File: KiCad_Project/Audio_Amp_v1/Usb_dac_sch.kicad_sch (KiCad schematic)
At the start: 40 parts, among them J1 Screw_Terminal_01x02, J2 Screw_Terminal_01x02, J3 Barrel_Jack_Switch, J6 USB_C_Receptacle_USB2.0_16P, Q1 NMOS, U1 PCM2704CDB, U2 USBLC6-2SC6, U4 L78L12_SOT89, Y1 12Mhz

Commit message: Started routing
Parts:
- removed C34: 10u, EEE-FK1H221GV:EEHZT1E561UV, symbol Device:C_Polarized_US
- removed Q1: NMOS, symbol Simulation_SPICE:NMOS
- added C34: 10u, Capacitor_SMD:C_0603_1608Metric, symbol Device:C
- added Q2: BSS138, Package_TO_SOT_SMD:SOT-23, symbol Transistor_FET:BSS138
- C30, C46: footprint Capacitor_SMD:C_0603_1608Metric -> Capacitor_SMD:C_0805_2012Metric
- C38, C40: footprint EEE-FK1H221GV:EEHZT1E561UV -> Capacitor_SMD:CP_Elec_4x5.8
- C43: footprint (none) -> PCM_JLCPCB:C_0805
- C44: footprint (none) -> Capacitor_SMD:C_0603_1608Metric
- C45: footprint (none) -> Capacitor_SMD:C_0805_2012Metric
- H1, H2, H3, H4: footprint (none) -> MountingHole:MountingHole_3.2mm_M3_Pad_Via
- J1, J2: footprint (none) -> TerminalBlock_Phoenix:TerminalBlock_Phoenix_MKDS-1,5-2-5.08_1x02_P5.08mm_Horizontal
- J3: footprint (none) -> Connector_BarrelJack:BarrelJack_CUI_PJ-102AH_Horizontal
- J6: footprint (none) -> Connector_USB:USB_C_Receptacle_GCT_USB4105-xx-A_16P_TopMnt_Horizontal
- XC1: renamed from Y1; footprint (none) -> Crystal:Crystal_SMD_HC49-SD; PARTNO (none) -> ECS-120-20-5PX-TR
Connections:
- net DAC_ACTIVE: now also Q2.1 (G)
- net GNDA: now also C34.1, Q2.2 (S)
- net OUT_N_LEFT: now also J2.1 (Pin_1); no longer J2.2 (Pin_2)
- net OUT_N_RIGHT: now also J1.1 (Pin_1); no longer J1.2 (Pin_2)
- net OUT_P_LEFT: now also J2.2 (Pin_2); no longer J2.1 (Pin_1)
- net OUT_P_RIGHT: now also J1.2 (Pin_2); no longer J1.1 (Pin_1)
- net at R17.1, R30.2: now also Q2.3 (D)
- net DAC_D+: now reaches R11.2, U1.9 (D+)
- net DAC_D-: now reaches R10.2, U1.8 (D-)
- net at U1.18 (VCOM): now also C34.2
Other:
- moved on the sheet: R21, TP4

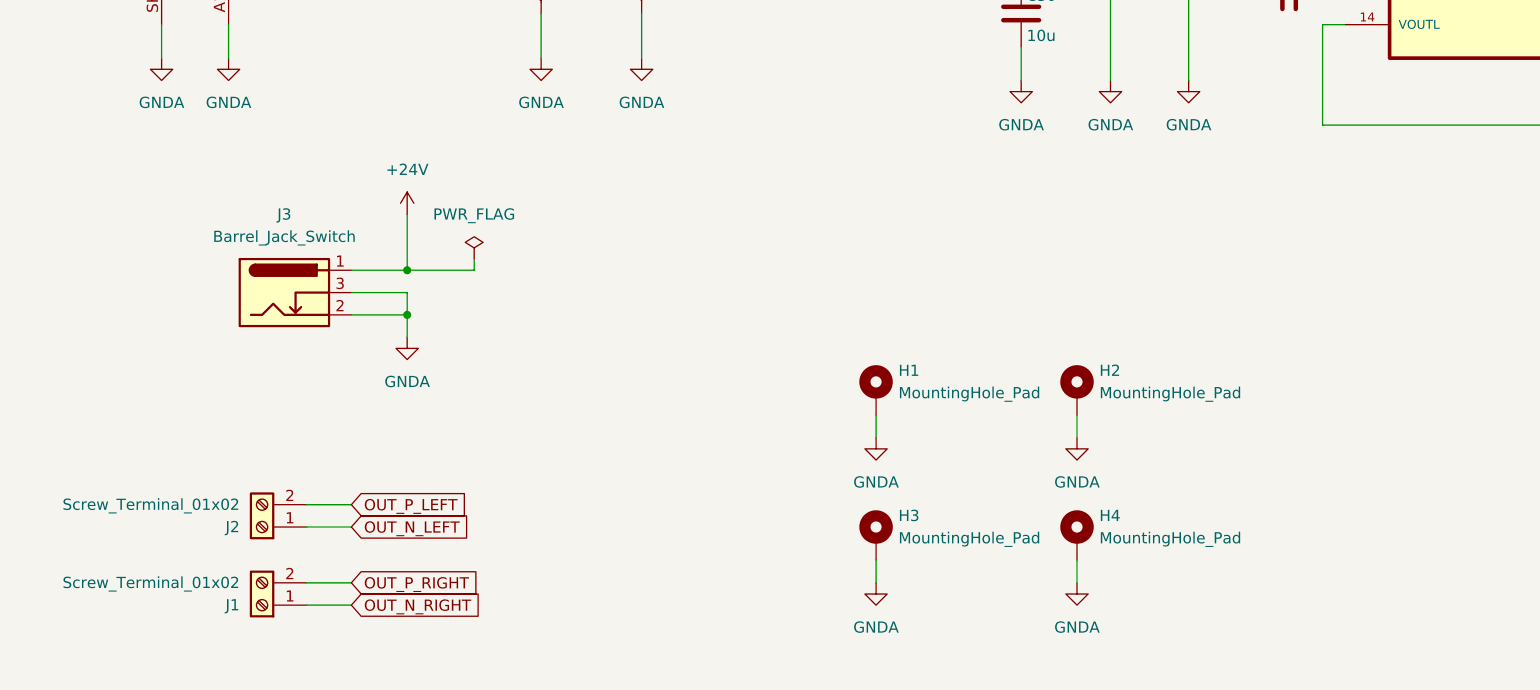
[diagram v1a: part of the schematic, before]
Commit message: added reverse polarity protection
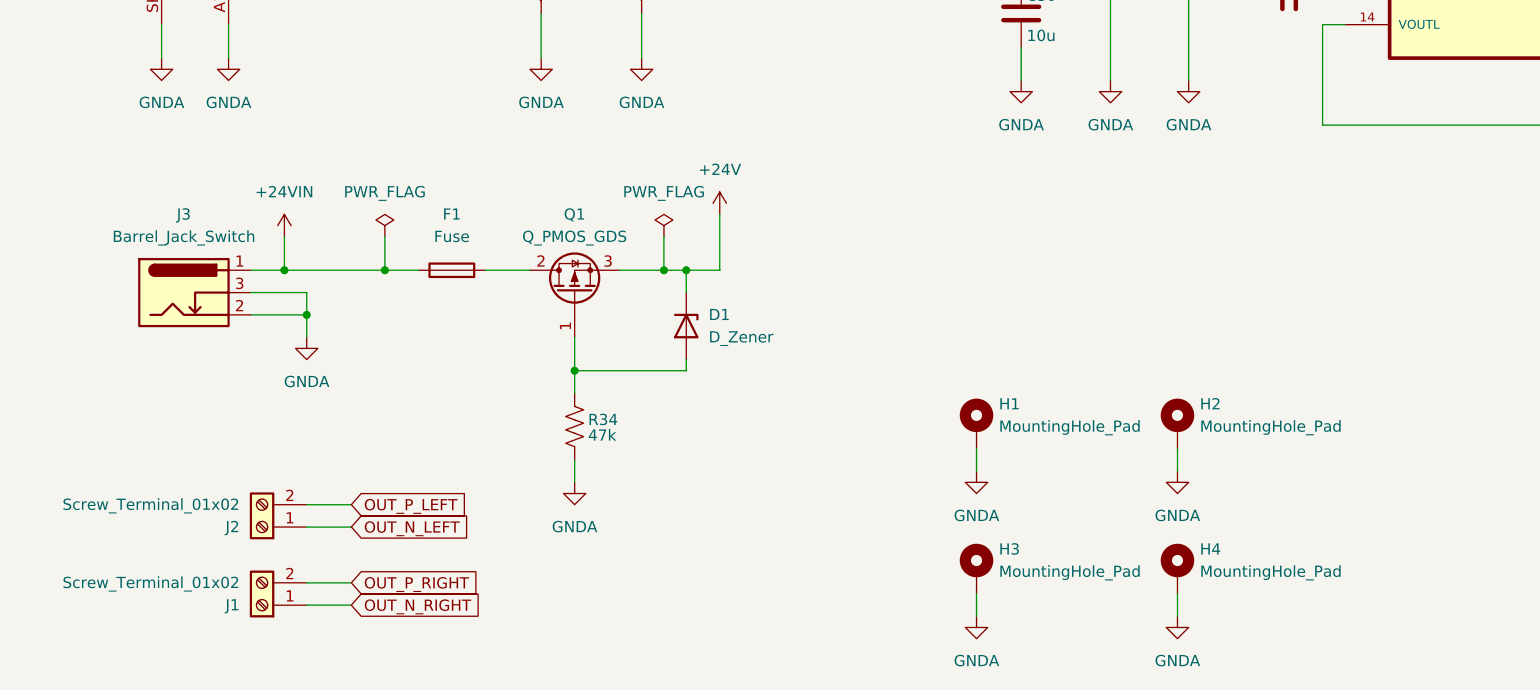
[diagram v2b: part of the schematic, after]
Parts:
- added D1: D_Zener, Diode_SMD:D_SOD-123, symbol Device:D_Zener
- added F1: Fuse, Fuse:Fuse_2920_7451Metric_Pad2.10x5.45mm_HandSolder, symbol Device:Fuse
- added Q1: Q_PMOS_GDS, Package_TO_SOT_SMD:TO-252-2, symbol Transistor_FET:Q_PMOS_GDS
- added R34: 47k, Resistor_SMD:R_0603_1608Metric, symbol Device:R_US
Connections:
- net +24V: now also D1.1 (K), Q1.3 (S); no longer J3.1
- net GNDA: now also R34.2
- new net: F1.2, Q1.2 (D)
- new net: D1.2 (A), Q1.1 (G), R34.1
- new net +24VIN: F1.1, J3.1
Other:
- moved on the sheet: H1, H2, H3, H4, J3

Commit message: Added led into pcb and lyout completed
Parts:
- added D2, D3, D4: LED, LED_SMD:LED_0805_2012Metric, symbol Device:LED
- added R15: 3k3, Resistor_SMD:R_0603_1608Metric, symbol Device:R_US
- added R18: 1k, Resistor_SMD:R_0603_1608Metric, symbol Device:R_US
- C30, C45: LCSC (none) -> C84416
- C32, C33, C37: LCSC (none) -> C5199872
- C34: LCSC (none) -> C962136
- C35, C36: LCSC (none) -> C5137624
- C38, C40: LCSC C116211 -> C445472
- C43: LCSC (none) -> C309049
- C44: LCSC (none) -> C5137636
- C46: LCSC (none) -> C2885646
- D1: LCSC (none) -> C2104
- F1: LCSC (none) -> C22870534
- J1, J2: LCSC (none) -> C480516
- J3: LCSC (none) -> C3096093
- J6: LCSC (none) -> C3020560
- Q1: LCSC (none) -> C513222
- Q2: LCSC (none) -> C52895
- R10, R11: LCSC C25586 -> C23345
- R14: LCSC C25586 -> C2930050
- R16: LCSC (none) -> C2907003
- R17, R19, R21, R34: LCSC C25586 -> C2907042
- R20: LCSC C25586 -> C98220
- R30: LCSC C25586 -> C14675
- R31, R32: LCSC C25586 -> C2907044
- U1: LCSC (none) -> C2859784
- U2: LCSC (none) -> C7519
- U4: LCSC (none) -> C915681
- XC1: LCSC (none) -> C5383154
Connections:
- net +12V: now also D2.2 (A)
- net GNDA: now also R15.2, R18.2
- net VBUS: now also D3.2 (A)
- net at Q2.3 (D), R30.2: now also D4.1 (K); no longer R17.1
- new net: D4.2 (A), R17.1
- new net: D3.1 (K), R18.1
- new net: D2.1 (K), R15.1
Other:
- moved on the sheet: R17

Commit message: added Images folder and changed some relative paths in the Kicad preferences
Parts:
- D3: LCSC C2293 -> C84256
- D4: LCSC C2297 -> C84256
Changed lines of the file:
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@@
 			)
 		)
-		(property "LCSC" "C2297"
+		(property "LCSC" "C84256"
 			(at 247.65 55.88 90)
 			(hide yes)
@@
 			)
 		)
-		(property "LCSC" "C2293"
+		(property "LCSC" "C84256"
 			(at 99.06 66.04 90)
 			(hide yes)

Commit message: Use shared Kicad_Libs instead of project-specific libraries
- Project parts moved to Kicad_Libs (symbol, footprint, 3D, datasheet)
- Lib tables point to ${KIPRJMOD}/../KiCad_Libs (link via bring_libs.bat)
- Schematic/PCB references (lib ids, footprints, 3D paths, datasheets)
  updated to the Kicad_Libs libraries; no design changes
- Removed the old project-specific library folder
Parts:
- U1: footprint PCM2704CDB:SOP65P780X200-28N -> eConverterADDA:SOP65P780X200-28N; symbol PCM2704CDB:PCM2704CDB -> eConverterADDA:PCM2704CDB
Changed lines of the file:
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@@
 	)
 	(symbol
-		(lib_id "PCM2704CDB:PCM2704CDB")
+		(lib_id "eConverterADDA:PCM2704CDB")
 		(at 189.23 86.36 0)
 		(unit 1)
@@
 			)
 		)
-		(property "Footprint" "PCM2704CDB:SOP65P780X200-28N"
+		(property "Footprint" "eConverterADDA:SOP65P780X200-28N"
 			(at 188.214 129.032 0)
 			(hide yes)
